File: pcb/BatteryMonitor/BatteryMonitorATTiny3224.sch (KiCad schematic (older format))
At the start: 26 parts, among them IC101 MAX3485E, IC102 ATTINY3224-SS, P101 RS485, P102 Bat, P103 Prog, U101 AMS1117, U103 MAX9918

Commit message: Working Board, tested over debug serial in DEVMODE
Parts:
- added R?: 270R, Resistors_SMD:R_0805, symbol R
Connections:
- net 5v: now also C106.2, C107.2; no longer C106.1, C107.1
- net GND: now also C106.1, C107.1; no longer C106.2, C107.2
- net UDPI: now also R?.2; no longer IC102.10 ((UDPI/RESET)_PA0)
- new net: IC102.10 ((UDPI/RESET)_PA0), R?.1
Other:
- note removed: "CPU"
- moved on the sheet: C106, C107
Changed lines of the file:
@@
 LIBS:contrib
 LIBS:valves
+LIBS:BatteryMonitorATTiny3224-cache
 EELAYER 25 0
 EELAYER END
@@
 L C C106
 U 1 1 6293FF59
-P 2900 1050
-F 0 "C106" H 2900 1150 40  0000 L CNN
-F 1 "100nF" H 2906 965 40  0000 L CNN
-F 2 "Capacitors_SMD:C_0805" H 2938 900 30  0001 C CNN
-F 3 "" H 2900 1050 60  0000 C CNN
-	1    2900 1050
+P 7700 2850
+F 0 "C106" H 7700 2950 40  0000 L CNN
+F 1 "100nF" H 7706 2765 40  0000 L CNN
+F 2 "Capacitors_SMD:C_0805" H 7738 2700 30  0001 C CNN
+F 3 "" H 7700 2850 60  0000 C CNN
+	1    7700 2850
 	1    0    0    -1
 $EndComp
@@
 L GND #PWR011
 U 1 1 629BB5D8
-P 2900 1350
-F 0 "#PWR011" H 2900 1350 30  0001 C CNN
-F 1 "GND" H 2900 1280 30  0001 C CNN
-F 2 "" H 2900 1350 60  0001 C CNN
-F 3 "" H 2900 1350 60  0001 C CNN
-	1    2900 1350
+P 7600 2600
+F 0 "#PWR011" H 7600 2600 30  0001 C CNN
+F 1 "GND" H 7600 2530 30  0001 C CNN
+F 2 "" H 7600 2600 60  0001 C CNN
+F 3 "" H 7600 2600 60  0001 C CNN
+	1    7600 2600
 	1    0    0    -1
 $EndComp
@@
 L C C107
 U 1 1 629CD333
-P 3150 1050
-F 0 "C107" H 3150 1150 40  0000 L CNN
-F 1 "1nF" H 3156 965 40  0000 L CNN
-F 2 "Capacitors_SMD:C_0805" H 3188 900 30  0001 C CNN
-F 3 "" H 3150 1050 60  0000 C CNN
-	1    3150 1050
-	1    0    0    -1
-$EndComp
-$Comp
-L GND #PWR013
-U 1 1 629CD46D
-P 3150 1350
-F 0 "#PWR013" H 3150 1350 30  0001 C CNN
-F 1 "GND" H 3150 1280 30  0001 C CNN
-F 2 "" H 3150 1350 60  0001 C CNN
-F 3 "" H 3150 1350 60  0001 C CNN
-	1    3150 1350
-	1    0    0    -1
-$EndComp
-Text Notes 2950 1550 0    60   ~ 0
-CPU
+P 7450 2850
+F 0 "C107" H 7450 2950 40  0000 L CNN
+F 1 "1nF" H 7456 2765 40  0000 L CNN
+F 2 "Capacitors_SMD:C_0805" H 7488 2700 30  0001 C CNN
+F 3 "" H 7450 2850 60  0000 C CNN
+	1    7450 2850
+	1    0    0    -1
+$EndComp
 Text Notes 1650 1550 0    60   ~ 0
 Other Chips as required
@@
 Text GLabel 9950 3650 2    60   Output ~ 0
 TXDebug
-Text GLabel 10000 3800 2    60   BiDi ~ 0
+Text GLabel 10550 3800 2    60   BiDi ~ 0
 UDPI
 Text GLabel 10600 4700 2    60   BiDi ~ 0
@@
 NoConn ~ 9950 3350
 Wire Wire Line
-	5000 3250 6050 3250
-Wire Wire Line
-	6050 3200 6050 3350
+	5000 3250 5750 3250
+Wire Wire Line
+	5750 3250 6050 3250
+Wire Wire Line
+	6050 3200 6050 3250
+Wire Wire Line
+	6050 3250 6050 3350
 Connection ~ 6050 3250
 Wire Wire Line
@@
 	6050 2650 6050 2700
 Wire Wire Line
-	4000 3450 4000 3650
+	4000 3450 4000 3550
+Wire Wire Line
+	4000 3550 4000 3650
 Wire Wire Line
 	4000 3450 4100 3450
@@
 	4850 4700 4750 4700
 Wire Wire Line
-	4750 4700 4750 4800
+	4750 4700 4750 4750
+Wire Wire Line
+	4750 4750 4750 4800
 Wire Wire Line
 	4750 4800 4850 4800
@@
 Connection ~ 4750 4750
 Wire Wire Line
-	3950 6250 3950 6400
-Wire Wire Line
-	3700 6300 4100 6300
+	3950 6250 3950 6300
+Wire Wire Line
+	3950 6300 3950 6400
+Wire Wire Line
+	3700 6300 3950 6300
+Wire Wire Line
+	3950 6300 4100 6300
 Connection ~ 3950 6300
 Wire Wire Line
@@
 	3700 7100 3950 7100
 Wire Wire Line
-	3950 6900 3950 7250
+	3950 6900 3950 7100
+Wire Wire Line
+	3950 7100 3950 7250
 Wire Wire Line
 	3750 5650 3950 5650
@@
 	1500 1000 1500 1100
 Wire Wire Line
-	750  700  1100 700
-Wire Wire Line
-	1900 700  3350 700
+	750  700  950  700
+Wire Wire Line
+	950  700  1100 700
+Wire Wire Line
+	1900 700  2000 700
+Wire Wire Line
+	2000 700  2350 700
+Wire Wire Line
+	2350 700  2650 700
+Wire Wire Line
+	2650 700  3350 700
 Wire Wire Line
 	950  800  950  700
@@
 Connection ~ 2350 700
 Wire Wire Line
-	2650 850  2650 700
+	2650 700  2650 850
 Connection ~ 2650 700
 Wire Wire Line
-	2900 850  2900 700
-Connection ~ 2900 700
-Wire Wire Line
 	2350 1250 2350 1400
 Wire Wire Line
 	2650 1250 2650 1350
 Wire Wire Line
-	2900 1250 2900 1350
-Wire Wire Line
-	3150 700  3150 850
-Wire Wire Line
-	3150 1250 3150 1350
-Connection ~ 3150 700
-Wire Wire Line
 	2900 2300 2900 2400
 Wire Wire Line
-	5050 3550 5050 4100
+	5050 3550 5050 3800
+Wire Wire Line
+	5050 3800 5050 4100
 Wire Wire Line
 	5050 3800 4850 3800
@@
 	10200 3200 9850 3200
 Wire Wire Line
-	7750 3200 7550 3200
+	7550 3200 7700 3200
+Wire Wire Line
+	7700 3200 7750 3200
 Wire Wire Line
 	7750 3350 7550 3350
@@
 	3250 5000 3250 4900
 Wire Wire Line
-	3250 4300 3250 4400
+	3250 4300 3250 4350
+Wire Wire Line
+	3250 4350 3250 4400
 Wire Wire Line
 	3250 3200 3250 3100
 Wire Wire Line
-	2750 3100 3800 3100
+	2750 3100 3250 3100
+Wire Wire Line
+	3250 3100 3500 3100
+Wire Wire Line
+	3500 3100 3800 3100
 Wire Wire Line
 	3800 3100 3800 3150
 Connection ~ 3250 3100
 Wire Wire Line
-	3800 3250 3800 4350
+	3800 4350 3800 3250
 Wire Wire Line
 	3250 3700 3250 3800
 Wire Wire Line
-	3800 4350 3250 4350
+	3250 4350 3500 4350
+Wire Wire Line
+	3500 4350 3800 4350
 Connection ~ 3250 4350
 Text Notes 3300 3800 0    60   ~ 0
@@
 	5300 3550 5300 3450
 Wire Wire Line
-	5000 3450 5550 3450
+	5000 3450 5300 3450
+Wire Wire Line
+	5300 3450 5550 3450
 $Comp
 L R R111
@@
 	3500 3500 3500 3100
 Connection ~ 3500 3100
+$Comp
+L R R?
+U 1 1 62AC3208
+P 10250 3800
+F 0 "R?" V 10330 3800 40  0000 C CNN
+F 1 "270R" V 10257 3801 40  0000 C CNN
+F 2 "Resistors_SMD:R_0805" V 10180 3800 30  0001 C CNN
+F 3 "" H 10250 3800 30  0000 C CNN
+	1    10250 3800
+	0    -1   -1   0
+$EndComp
+Wire Wire Line
+	10500 3800 10550 3800
+Wire Wire Line
+	7700 3050 7700 3100
+Wire Wire Line
+	7700 3100 7700 3200
+Connection ~ 7700 3200
+Wire Wire Line
+	7700 2450 7700 2650
+Wire Wire Line
+	7450 2450 7600 2450
+Wire Wire Line
+	7600 2450 7700 2450
+Wire Wire Line
+	7700 3100 7450 3100
+Wire Wire Line
+	7450 3100 7450 3050
+Connection ~ 7700 3100
+Wire Wire Line
+	7450 2650 7450 2450
+Wire Wire Line
+	7600 2450 7600 2600
+Connection ~ 7600 2450
 $EndSCHEMATC

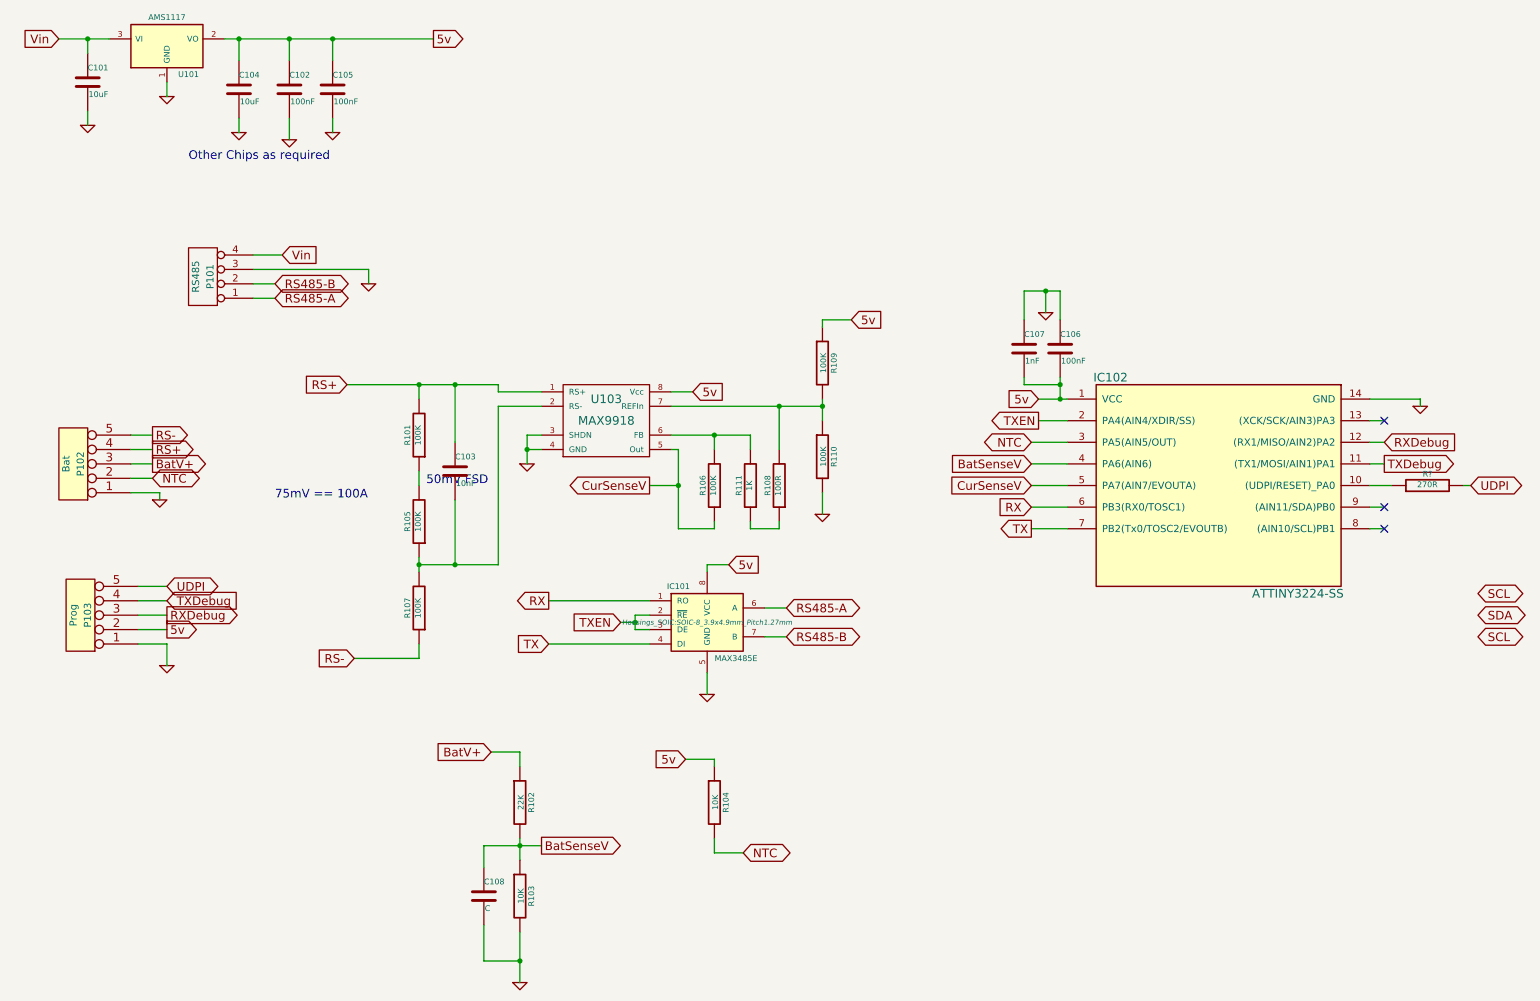
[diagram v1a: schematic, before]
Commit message: Eliminated current Amp, using only Attiny3224 ADC
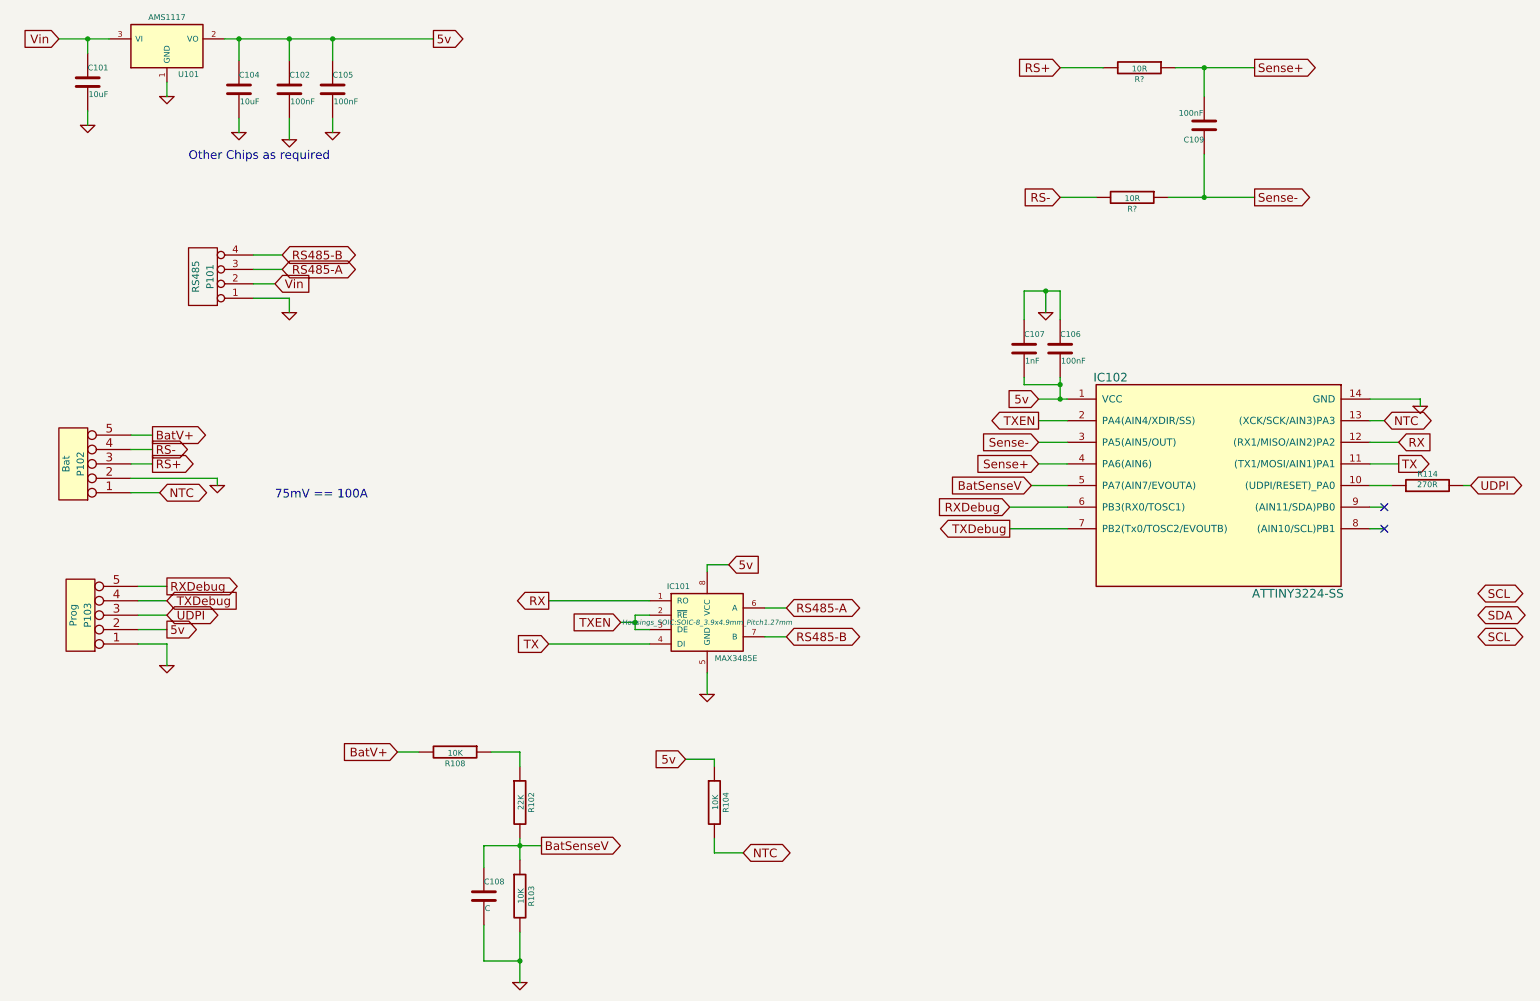
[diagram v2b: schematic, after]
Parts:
- removed C103: 10nF, Capacitors_SMD:C_0805, symbol C
- removed R101, R105, R106, R107, R109, R110: 100K, Resistors_SMD:R_0805, symbol R
- removed R111: 1K, Resistors_SMD:R_0805, symbol R
- removed U103: MAX9918, Housings_SOIC:SOIC-8_3.9x4.9mm_Pitch1.27mm, symbol MAX9918
- added C109: 100nF, Capacitors_SMD:C_0805, symbol C
- added R? (x2): 10R, Resistors_SMD:R_0805, symbol R
- R108: value 100R -> 10K
- gave numbers to parts that had none: 1
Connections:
- net CurSenseV is gone; now on net BatSenseV: IC102.5 (PA7(AIN7/EVOUTA))
- net BatSenseV: no longer IC102.4 (PA6(AIN6))
- net BatV+: now also P102.5, R108.2; no longer P102.3, R102.1
- net GND: now also P101.1 (P1), P102.2; no longer P101.3 (P3), P102.1
- net NTC: now also IC102.13 ((XCK/SCK/AIN3)PA3), P102.1; no longer IC102.3 (PA5(AIN5/OUT)), P102.2
- net RS+: now also P102.3, R?.2; no longer P102.4
- net RS-: now also P102.4, R?.2; no longer P102.5
- net RS485-A: now also P101.3 (P3); no longer P101.1 (P1)
- net RS485-B: now also P101.4 (P4); no longer P101.2 (P2)
- net RX: now also IC102.12 ((RX1/MISO/AIN2)PA2); no longer IC102.6 (PB3(RX0/TOSC1))
- net RXDebug: now also IC102.6 (PB3(RX0/TOSC1)), P103.5; no longer IC102.12 ((RX1/MISO/AIN2)PA2), P103.3
- net TX: now also IC102.11 ((TX1/MOSI/AIN1)PA1); no longer IC102.7 (PB2(Tx0/TOSC2/EVOUTB))
- net TXDebug: now also IC102.7 (PB2(Tx0/TOSC2/EVOUTB)); no longer IC102.11 ((TX1/MOSI/AIN1)PA1)
- net UDPI: now also P103.3; no longer P103.5
- net Vin: now also P101.2 (P2); no longer P101.4 (P4)
- net at R108.1: now also R102.1
- new net Sense+: C109.2, IC102.4 (PA6(AIN6)), R?.1
- new net Sense-: C109.1, IC102.3 (PA5(AIN5/OUT)), R?.1
- no-connect marks 3 -> 2
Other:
- note removed: "50mV FSD"
